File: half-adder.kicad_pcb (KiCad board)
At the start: 2 copper layers, 53 parts, among them J1 A, J2 B, J3 C, J4 OUTPUT, J5 CARRY OUT, Q1 BC547, Q10 BC547, Q11 BC547, Q12 BC547, Q13 BC547, Q14 BC547, Q15 BC547, Q16 BC547, Q17 BC547, Q18 BC547, Q19 BC547, Q2 BC547, Q20 BC547, Q21 BC547, Q22 BC547, Q23 BC547, Q24 BC547, Q25 BC547, Q3 BC547, Q4 BC547, Q5 BC547, Q6 BC547, Q7 BC547, Q8 BC547, Q9 BC547

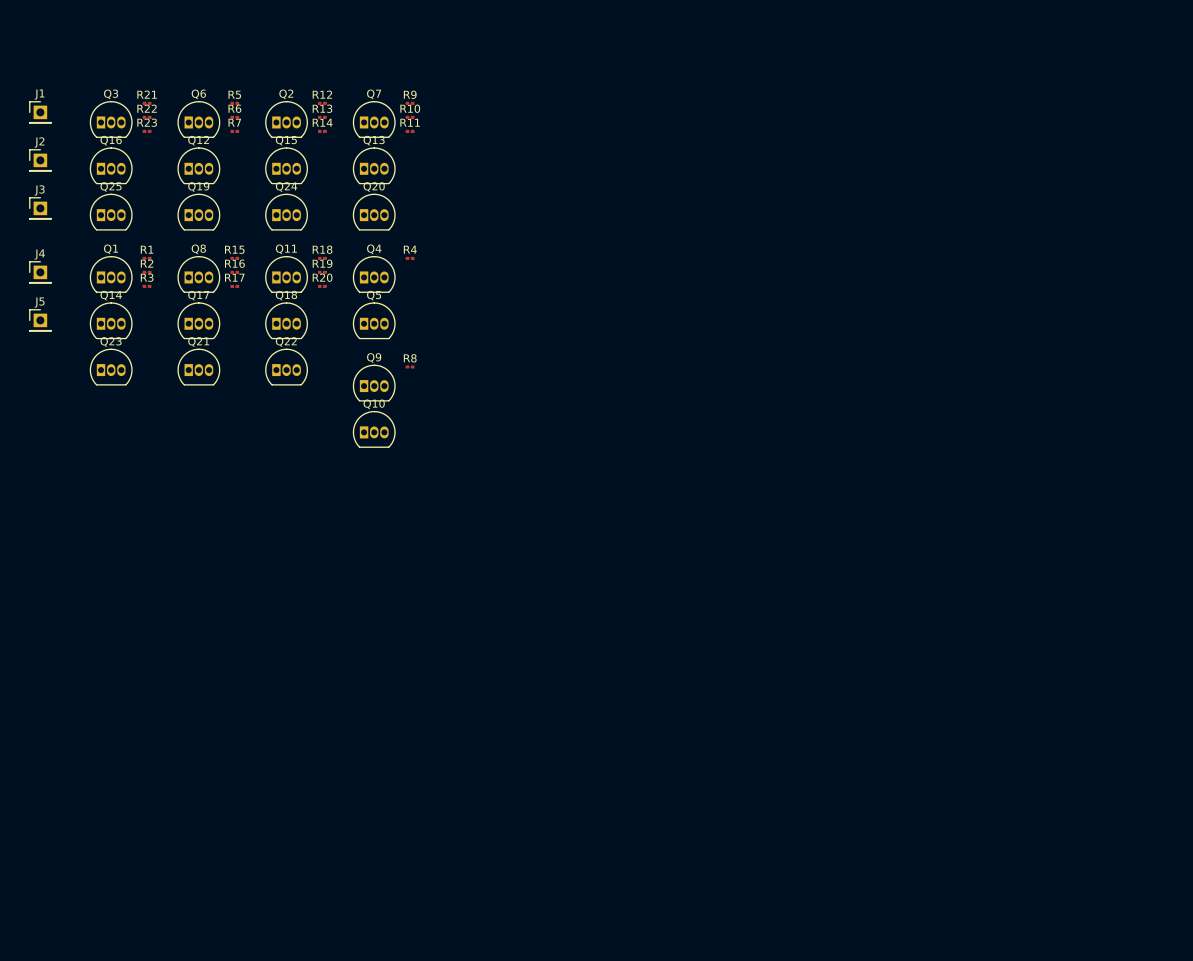
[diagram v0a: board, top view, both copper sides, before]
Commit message: Fix design rule checker errors
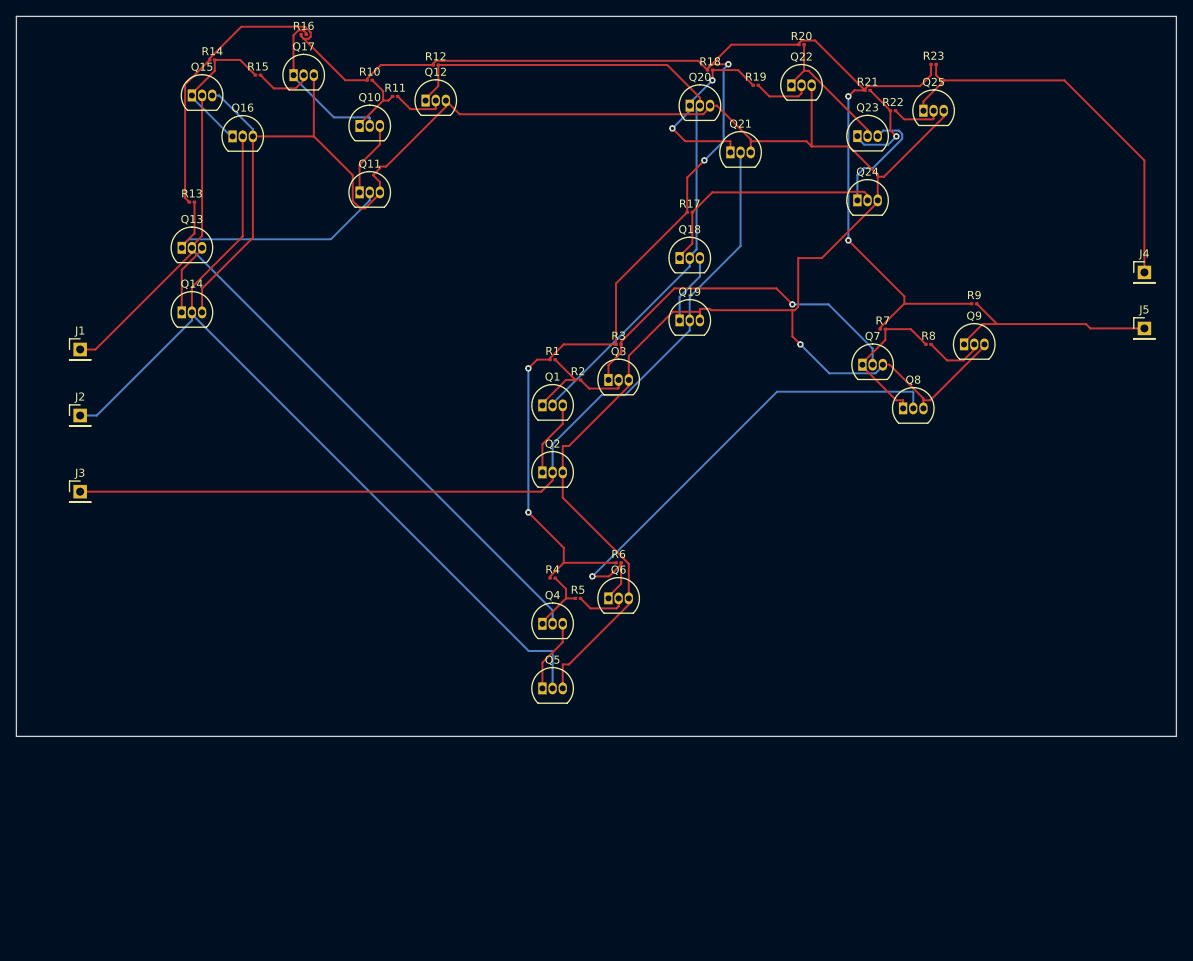
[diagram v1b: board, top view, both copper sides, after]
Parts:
- moved J5 138.0 mm to (155.0, 52.0)
- moved J4 138.0 mm to (155.0, 45.0)
- moved Q25 103.6 mm to (127.4, 24.8)
- moved Q23 99.0 mm to (119.1, 28.0)
- moved R23 98.7 mm to (128.7, 19.0)
- moved R22 93.2 mm to (123.6, 24.8)
- moved Q8 90.8 mm to (124.8, 62.0)
- moved R21 90.1 mm to (120.4, 22.2)
- moved R7 84.7 mm to (122.3, 52.1)
- moved Q6 79.3 mm to (88.0, 85.8)
- moved R5 75.3 mm to (84.2, 85.8)
- moved Q9 75.2 mm to (132.5, 54.0)
- moved R9 74.8 mm to (133.7, 48.9)
- moved Q22 73.6 mm to (110.9, 21.6)
- moved R6 73.5 mm to (89.3, 81.3)
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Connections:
- J1 pad 1: /xor-gate/A -> Net-(J1-Pin_1)
- J2 pad 1: /and-gate/B -> Net-(J2-Pin_1)
- J3 pad 1: /and-gate1/B -> Net-(J3-Pin_1)
- J4 pad 1: /xor-gate1/OUTPUT -> Net-(J4-Pin_1)
- J5 pad 1: /or-gate/OUTPUT -> Net-(J5-Pin_1)
- Q1 pad 1: /xor-gate/and-gate/A -> Net-(Q1-C)
- Q1 pad 3: GND -> Net-(Q1-E)
- Q10 pad 2: /and-gate1/B -> Net-(Q10-B)
- Q10 pad 3: GND -> Net-(Q10-E)
- Q11 pad 1: /and-gate1/OUTPUT -> Net-(Q10-E)
- Q12 pad 1: Net-(Q12-C) -> Net-(Q1-B)
- Q12 pad 2: /xor-gate/and-gate/B -> Net-(Q12-B)
- Q13 pad 1: Net-(Q13-C) -> Net-(Q11-B)
- Q13 pad 2: /xor-gate1/and-gate/B -> Net-(J1-Pin_1)
- Q13 pad 3: GND -> Net-(Q13-E)
- Q14 pad 1: Net-(Q14-C) -> Net-(Q13-E)
- Q14 pad 2: /and-gate/B -> Net-(J2-Pin_1)
- Q15 pad 2: /and-gate1/B -> Net-(J1-Pin_1)
- Q16 pad 1: Net-(Q16-C) -> Net-(Q15-C)
- Q16 pad 2: /and-gate/OUTPUT -> Net-(J2-Pin_1)
- Q17 pad 1: Net-(Q17-C) -> Net-(Q10-B)
- Q17 pad 2: /and-gate/B -> Net-(Q17-B)
- Q18 pad 2: /and-gate1/B -> Net-(Q1-B)
- Q18 pad 3: GND -> Net-(Q18-E)
- Q19 pad 1: Net-(Q19-C) -> Net-(Q18-E)
- Q19 pad 2: /xor-gate/and-gate/A -> Net-(J3-Pin_1)
- Q19 pad 3: Net-(Q12-C) -> GND
- Q2 pad 1: /xor-gate1/and-gate/A -> Net-(Q1-E)
- Q2 pad 2: Net-(Q2-B) -> Net-(J3-Pin_1)
- Q20 pad 2: /xor-gate1/and-gate/A -> Net-(Q1-B)
- Q20 pad 3: Net-(Q13-C) -> GND
- Q21 pad 1: Net-(Q21-C) -> Net-(Q20-C)
- Q21 pad 2: /and-gate/A -> Net-(J3-Pin_1)
- Q21 pad 3: Net-(Q17-C) -> GND
- Q22 pad 2: /and-gate1/A -> Net-(Q22-B)
- Q22 pad 3: Net-(Q18-C) -> GND
- Q23 pad 1: Net-(Q14-C) -> Net-(Q23-C)
- Q23 pad 2: /xor-gate/A -> Net-(Q22-C)
- Q23 pad 3: GND -> Net-(Q23-E)
- Q24 pad 1: Net-(Q15-C) -> Net-(Q23-E)
- Q24 pad 2: /and-gate1/A -> Net-(Q18-C)
- Q25 pad 1: Net-(Q16-C) -> Net-(J4-Pin_1)
- Q25 pad 2: /and-gate1/OUTPUT -> Net-(Q25-B)
- Q3 pad 1: /or-gate/OUTPUT -> Net-(Q3-C)
- Q4 pad 1: /xor-gate/and-gate/B -> Net-(Q4-C)
- Q4 pad 2: /xor-gate/A -> Net-(J1-Pin_1)
- Q5 pad 2: /and-gate/B -> Net-(J2-Pin_1)
- Q6 pad 1: /xor-gate/OUTPUT -> Net-(Q6-C)
- Q7 pad 1: /xor-gate1/OUTPUT -> Net-(Q7-C)
- Q7 pad 2: Net-(Q7-B) -> Net-(Q3-C)
- Q8 pad 1: /and-gate/OUTPUT -> Net-(Q7-C)
- Q8 pad 2: Net-(Q8-B) -> Net-(Q6-C)
- Q9 pad 1: /xor-gate1/and-gate/B -> Net-(J5-Pin_1)
- Q9 pad 2: /and-gate1/A -> Net-(Q9-B)
- Q9 pad 3: Net-(Q10-C) -> GND
- R1 pad 2: Net-(Q14-C) -> Net-(Q1-C)
- R10 pad 1: Net-(Q20-C) -> +5V
- R10 pad 2: Net-(Q7-B) -> Net-(Q10-C)
- R11 pad 1: +5V -> Net-(Q10-C)
- R11 pad 2: /xor-gate1/OUTPUT -> Net-(Q12-B)
- R12 pad 2: Net-(Q15-C) -> Net-(Q1-B)
- R13 pad 1: Net-(Q15-C) -> +5V
- R13 pad 2: Net-(Q2-B) -> Net-(Q11-B)
- R14 pad 2: /xor-gate1/and-gate/A -> Net-(Q15-C)
- R15 pad 1: +5V -> Net-(Q15-C)
- R15 pad 2: Net-(Q21-C) -> Net-(Q17-B)
- R16 pad 1: Net-(Q21-C) -> +5V
- R16 pad 2: Net-(Q8-B) -> Net-(Q10-B)
- R17 pad 2: /and-gate/OUTPUT -> Net-(Q18-C)
- R18 pad 2: Net-(Q22-C) -> Net-(Q20-C)
- R19 pad 1: Net-(Q22-C) -> Net-(Q20-C)
- R19 pad 2: Net-(Q11-B) -> Net-(Q22-B)
- R2 pad 1: Net-(Q14-C) -> Net-(Q1-C)
- R2 pad 2: Net-(Q1-B) -> Net-(Q3-B)
- R20 pad 2: /and-gate1/OUTPUT -> Net-(Q22-C)
- R21 pad 2: Net-(Q16-C) -> Net-(Q23-C)
- R22 pad 1: Net-(Q16-C) -> Net-(Q23-C)
- R22 pad 2: Net-(Q3-B) -> Net-(Q25-B)
- R23 pad 2: /or-gate/OUTPUT -> Net-(J4-Pin_1)
- R3 pad 2: /xor-gate/and-gate/A -> Net-(Q3-C)
- R4 pad 2: /xor-gate/and-gate/B -> Net-(Q4-C)
- R5 pad 1: +5V -> Net-(Q4-C)
- R5 pad 2: Net-(Q19-C) -> Net-(Q6-B)
- R6 pad 1: Net-(Q19-C) -> +5V
- R6 pad 2: Net-(Q6-B) -> Net-(Q6-C)
- R7 pad 2: /xor-gate/OUTPUT -> Net-(Q7-C)
- R8 pad 1: +5V -> Net-(Q7-C)
- R8 pad 2: /xor-gate1/and-gate/B -> Net-(Q9-B)
- R9 pad 2: Net-(Q20-C) -> Net-(J5-Pin_1)
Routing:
- net GND: track 0.00 -> 295.6 mm, vias 0 -> 1
- net +5V: track 0.00 -> 261.0 mm, vias 0 -> 6
- net Net-(J2-Pin_1): track 0.00 -> 112.7 mm
- net Net-(J3-Pin_1): track 0.00 -> 112.1 mm
- net Net-(J1-Pin_1): track 0.00 -> 104.9 mm
- net Net-(Q1-B): track 0.00 -> 85.6 mm
- net Net-(Q6-C): track 0.00 -> 61.7 mm, vias 0 -> 1
- net Net-(J4-Pin_1): track 0.00 -> 50.7 mm
- net Net-(Q3-C): track 0.00 -> 46.0 mm, vias 0 -> 1
- net Net-(Q11-B): track 0.00 -> 33.4 mm
- net Net-(Q18-C): track 0.00 -> 30.2 mm
- net Net-(J5-Pin_1): track 0.00 -> 27.6 mm
- net Net-(Q20-C): track 0.00 -> 24.6 mm, vias 0 -> 2
- net Net-(Q10-B): track 0.00 -> 20.3 mm
- net Net-(Q7-C): track 0.00 -> 19.6 mm
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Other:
- board outline added: 145 x 90 mm

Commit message: Change resistors to more common type
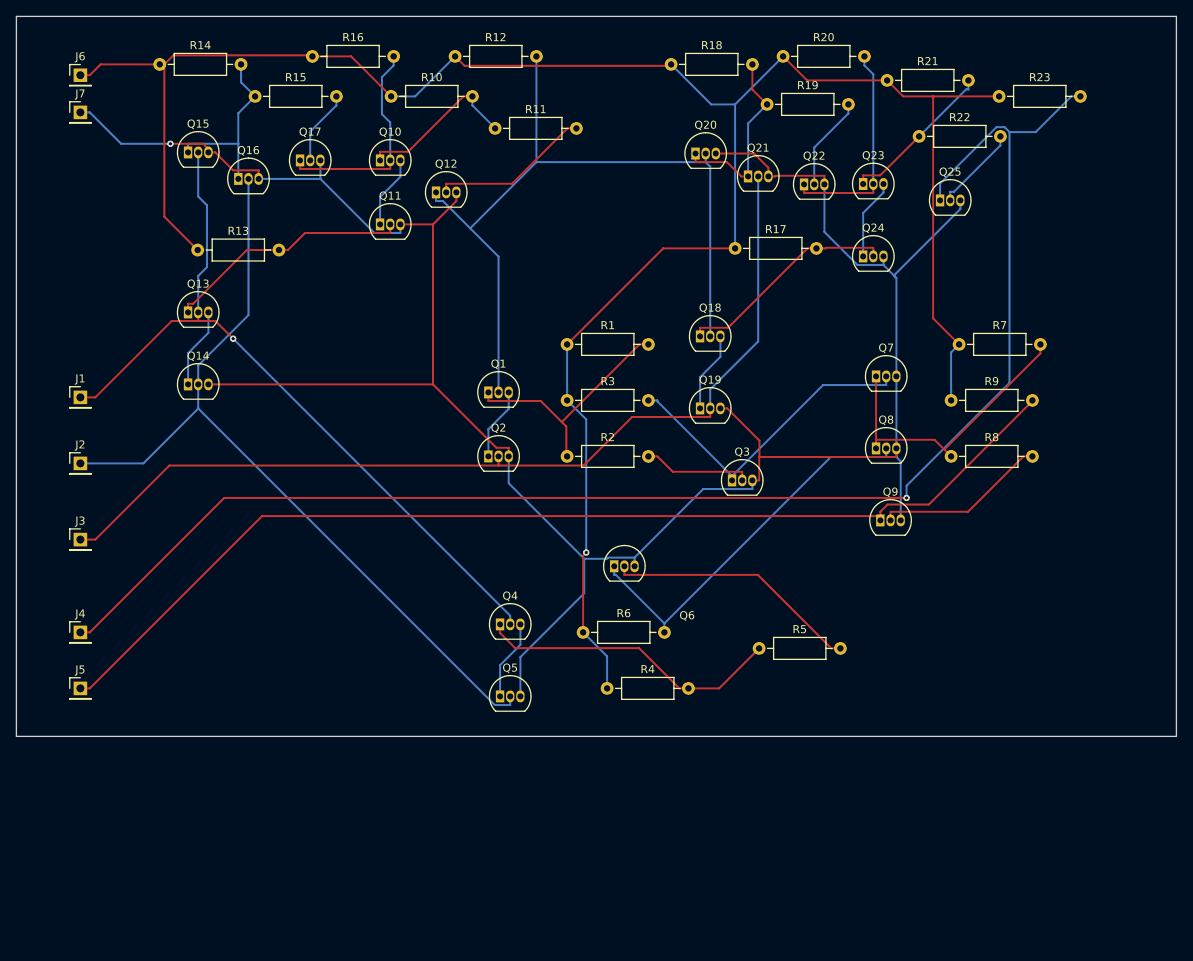
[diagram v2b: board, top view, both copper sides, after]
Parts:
- added J6: 5V, Connector_PinHeader_2.54mm:PinHeader_1x01_P2.54mm_Vertical, F.Cu at (22.0, 20.4)
- added J7: GROUND, Connector_PinHeader_2.54mm:PinHeader_1x01_P2.54mm_Vertical, F.Cu at (22.0, 25.0)
- R1, R10, R11, R12, R13, R14, R15, R16, R17, R18, R19, R2, R20, R21, R22, R23, R3, R4, R5, R6, R7, R8, R9: footprint Resistor_SMD:R_0201_0603Metric -> Resistor_THT:R_Axial_DIN0207_L6.3mm_D2.5mm_P10.16mm_Horizontal
- moved J4 140.4 mm to (22.0, 90.0)
- moved J5 140.4 mm to (22.0, 97.0)
- moved Q9 24.4 mm to (122.0, 76.0)
- moved R5 23.5 mm to (106.8, 92.0)
- moved Q3 19.9 mm to (103.5, 71.0)
- moved R4 15.4 mm to (87.8, 97.0)
- moved R8 14.3 mm to (130.8, 68.0)
- moved R11 13.1 mm to (73.8, 27.0)
- moved Q22 12.5 mm to (112.5, 34.0)
- moved R9 12.4 mm to (130.8, 61.0)
- moved Q12 11.6 mm to (66.5, 35.0)
- moved Q25 11.4 mm to (129.5, 36.0)
- moved Q19 11.3 mm to (99.5, 62.0)
- moved Q17 10.7 mm to (49.5, 31.0)
- moved Q18 10.1 mm to (99.5, 53.0)
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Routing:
- net Net-(J4-Pin_1): track 50.7 -> 186.0 mm, vias 0 -> 1
- net Net-(J5-Pin_1): track 27.6 -> 134.9 mm
- net Net-(Q4-C): track 8.95 -> 38.4 mm
- net Net-(Q6-B): track 6.38 -> 31.9 mm
- net Net-(Q1-C): track 9.16 -> 30.8 mm
- net +5V: track 261.0 -> 281.3 mm, vias 6 -> 1
- net Net-(Q7-C): track 19.6 -> 37.4 mm
- net Net-(Q9-B): track 7.44 -> 21.7 mm
- net Net-(Q12-B): track 6.45 -> 20.2 mm
- net Net-(Q6-C): track 61.7 -> 48.4 mm, vias 1 -> 0
- net Net-(Q1-B): track 85.6 -> 97.9 mm
- net Net-(Q10-C): track 8.89 -> 20.7 mm
- net Net-(Q22-C): track 17.5 -> 27.2 mm
- net Net-(J1-Pin_1): track 104.9 -> 96.0 mm, vias 0 -> 1
- net Net-(J2-Pin_1): track 112.7 -> 104.3 mm
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
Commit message: Ngspice simulation
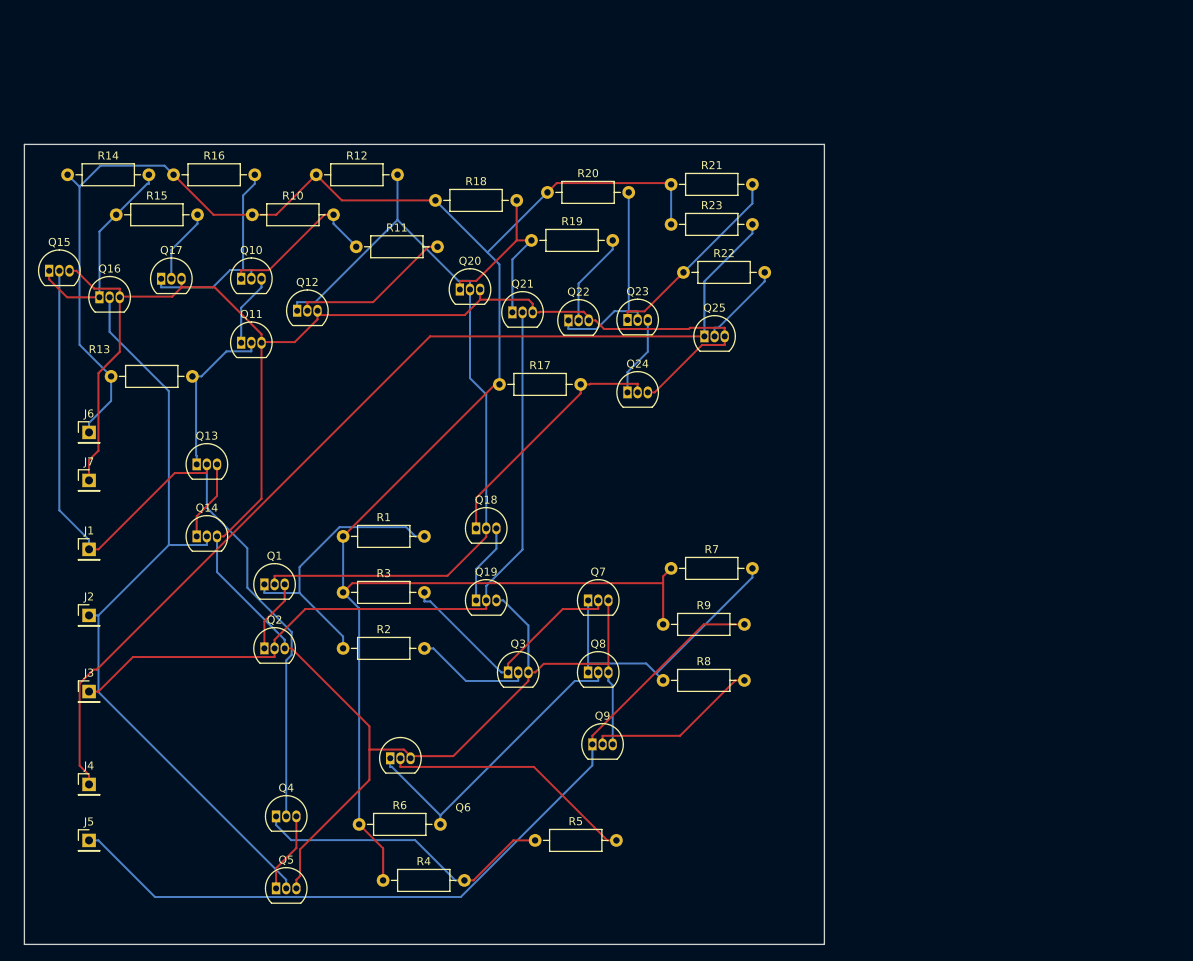
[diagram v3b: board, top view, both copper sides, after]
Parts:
- R1, R14: value R -> 330
- moved J7 46.0 mm to (23.1, 71.0)
- moved Q7 45.6 mm to (85.5, 86.0)
- moved Q8 45.6 mm to (85.5, 95.0)
- moved Q9 45.6 mm to (86.0, 104.0)
- moved R7 45.6 mm to (95.8, 82.0)
- moved R8 45.6 mm to (94.8, 96.0)
- moved R9 45.6 mm to (94.8, 89.0)
- moved J6 44.7 mm to (23.1, 65.0)
- moved R23 44.0 mm to (95.8, 39.0)
- moved Q1 36.9 mm to (45.0, 84.0)
- moved Q18 36.9 mm to (71.5, 77.0)
- moved Q19 36.9 mm to (71.5, 86.0)
- moved Q2 36.9 mm to (45.0, 92.0)
- moved Q3 36.9 mm to (75.5, 95.0)
- moved Q6 36.9 mm to (60.7, 105.7)
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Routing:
- net Net-(J4-Pin_1): track 186.0 -> 125.6 mm, vias 1 -> 0
- net Net-(J5-Pin_1): track 134.9 -> 101.1 mm
- net Net-(J3-Pin_1): track 118.8 -> 94.1 mm
- net +5V: track 281.3 -> 265.4 mm, vias 1 -> 0
- net GND: track 294.7 -> 283.1 mm, vias 1 -> 0
- net Net-(Q11-B): track 31.1 -> 20.8 mm
- net Net-(Q6-C): track 48.4 -> 38.7 mm
- net Net-(J1-Pin_1): track 96.0 -> 104.8 mm, vias 1 -> 0
- net Net-(Q3-C): track 40.1 -> 31.5 mm
- net Net-(J2-Pin_1): track 104.3 -> 97.3 mm
- net Net-(Q1-C): track 30.8 -> 36.0 mm
- net Net-(Q23-C): track 19.8 -> 24.7 mm
- net Net-(Q18-C): track 28.0 -> 31.6 mm
- net Net-(Q15-C): track 23.3 -> 26.3 mm
- net Net-(Q20-C): track 24.1 -> 27.1 mm
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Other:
- board size 145 x 90 mm -> 100 x 100 mm
